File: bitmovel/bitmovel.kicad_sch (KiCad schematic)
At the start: 19 parts, among them J1 Conn_01x02_Male, J2 micro:bit, J3 motor D, J4 motor E, J5 Conn_01x02_Female, J6 Conn_01x02_Female, J7 Conn_01x01_Female, J8 Conn_01x01_Female, SW1 SW_SPST, U1 LM1117-3.3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

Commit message: Inclui ilhas para conectar a Vin
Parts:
- added J9: Conn_01x02_Female, Connector_PinHeader_2.54mm:PinHeader_1x02_P2.54mm_Vertical, symbol Connector:Conn_01x02_Female
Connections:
- net Vin: now also J9.1 (Pin_1), J9.2 (Pin_2)
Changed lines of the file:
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@@
+    (stroke (width 0) (type default) (color 0 0 0 0))
+  )
+  (wire (pts (xy 115.57 103.505) (xy 115.57 106.045))
     (stroke (width 0) (type default) (color 0 0 0 0))
   )
@@
   )
   (label "3.3V" (at 147.32 113.03 0)
+    (effects (font (size 1.27 1.27)) (justify left bottom))
+  )
+  (label "Vin" (at 115.57 105.41 0)
     (effects (font (size 1.27 1.27)) (justify left bottom))
   )
@@
     (pin "1")
   )
+  (symbol (lib_id "Connector:Conn_01x02_Female") (at 110.49 103.505 0) (mirror y) (unit 1)
+    (in_bom yes) (on_board yes) (fields_autoplaced)
+    (property "Reference" "J9" (id 0) (at 111.125 97.79 0)
+      (effects (font (size 1.27 1.27)) hide)
+    )
+    (property "Value" "Conn_01x02_Female" (id 1) (at 111.125 100.33 0)
+      (effects (font (size 1.27 1.27)) hide)
+    )
+    (property "Footprint" "Connector_PinHeader_2.54mm:PinHeader_1x02_P2.54mm_Vertical" (id 2) (at 110.49 103.505 0)
+      (effects (font (size 1.27 1.27)) hide)
+    )
+    (property "Datasheet" "~" (id 3) (at 110.49 103.505 0)
+      (effects (font (size 1.27 1.27)) hide)
+    )
+    (pin "1")
+    (pin "2")
+  )
   (symbol (lib_id "Connector:Conn_01x02_Female") (at 110.49 116.205 0) (mirror y) (unit 1)
     (in_bom yes) (on_board yes) (fields_autoplaced)
@@
       (reference "J8") (unit 1) (value "Conn_01x01_Female") (footprint "Connector_PinHeader_2.54mm:PinHeader_1x01_P2.54mm_Vertical")
     )
+    (path "/dde3811c-ee13-425b-b5d6-76051d186440"
+      (reference "J9") (unit 1) (value "Conn_01x02_Female") (footprint "Connector_PinHeader_2.54mm:PinHeader_1x02_P2.54mm_Vertical")
+    )
     (path "/00000000-0000-0000-0000-00005ffbb56c"

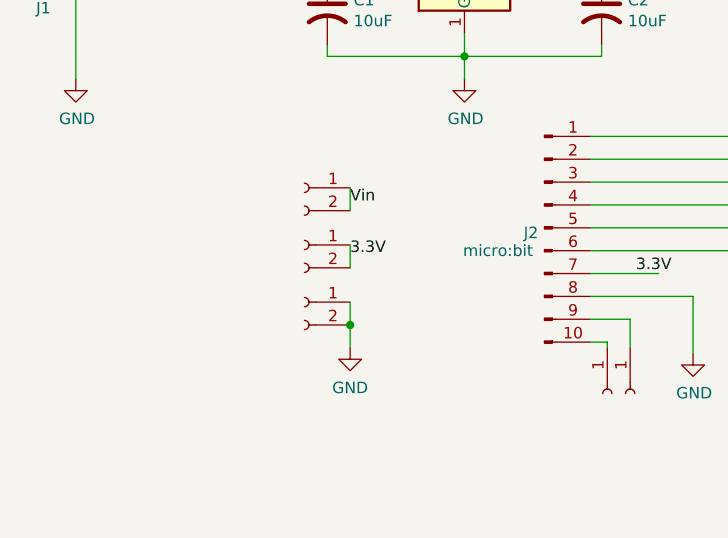
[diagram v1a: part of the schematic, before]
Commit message: Corrige posição das ilhas 3v3 e GND
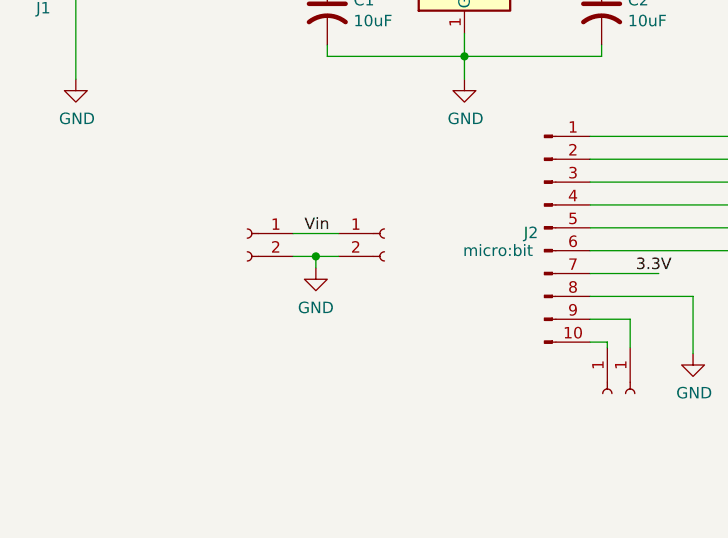
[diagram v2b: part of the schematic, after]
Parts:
- removed J5: Conn_01x02_Female, Connector_PinHeader_2.54mm:PinHeader_1x02_P2.54mm_Vertical, symbol Connector:Conn_01x02_Female
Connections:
- net GND: now also J9.2 (Pin_2); no longer J6.1 (Pin_1)
- net Vin: now also J6.1 (Pin_1); no longer J9.2 (Pin_2)
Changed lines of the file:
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@@
   (junction (at 128.27 88.9) (diameter 0) (color 0 0 0 0)
   )
-  (junction (at 115.57 118.745) (diameter 0) (color 0 0 0 0)
-  )
   (junction (at 113.03 78.74) (diameter 0) (color 0 0 0 0)
   )
@@
   (junction (at 147.32 69.85) (diameter 0) (color 0 0 0 0)
   )
+  (junction (at 111.76 111.125) (diameter 0) (color 0 0 0 0)
+  )
   (junction (at 175.26 129.54) (diameter 0) (color 0 0 0 0)
   )
@@
     (stroke (width 0) (type default) (color 0 0 0 0))
   )
-  (wire (pts (xy 115.57 116.205) (xy 115.57 118.745))
-    (stroke (width 0) (type default) (color 0 0 0 0))
-  )
   (wire (pts (xy 146.685 118.11) (xy 146.685 121.285))
     (stroke (width 0) (type default) (color 0 0 0 0))
   )
+  (wire (pts (xy 111.76 112.395) (xy 111.76 111.125))
+    (stroke (width 0) (type default) (color 0 0 0 0))
+  )
   (wire (pts (xy 113.03 78.74) (xy 113.03 69.85))
     (stroke (width 0) (type default) (color 0 0 0 0))
@@
     (stroke (width 0) (type default) (color 0 0 0 0))
   )
+  (wire (pts (xy 111.76 111.125) (xy 114.3 111.125))
+    (stroke (width 0) (type default) (color 0 0 0 0))
+  )
   (wire (pts (xy 142.24 110.49) (xy 158.75 110.49))
     (stroke (width 0) (type default) (color 0 0 0 0))
@@
     (stroke (width 0) (type default) (color 0 0 0 0))
   )
-  (wire (pts (xy 115.57 109.855) (xy 115.57 112.395))
-    (stroke (width 0) (type default) (color 0 0 0 0))
-  )
   (wire (pts (xy 182.88 129.54) (xy 182.88 128.27))
     (stroke (width 0) (type default) (color 0 0 0 0))
@@
     (stroke (width 0) (type default) (color 0 0 0 0))
   )
+  (wire (pts (xy 109.22 108.585) (xy 114.3 108.585))
+    (stroke (width 0) (type default) (color 0 0 0 0))
+  )
   (wire (pts (xy 172.72 129.54) (xy 175.26 129.54))
     (stroke (width 0) (type default) (color 0 0 0 0))
@@
     (stroke (width 0) (type default) (color 0 0 0 0))
   )
-  (wire (pts (xy 115.57 118.745) (xy 115.57 121.285))
-    (stroke (width 0) (type default) (color 0 0 0 0))
-  )
   (wire (pts (xy 161.29 92.71) (xy 165.1 92.71))
     (stroke (width 0) (type default) (color 0 0 0 0))
@@
     (stroke (width 0) (type default) (color 0 0 0 0))
   )
-  (wire (pts (xy 115.57 103.505) (xy 115.57 106.045))
-    (stroke (width 0) (type default) (color 0 0 0 0))
-  )
   (wire (pts (xy 190.5 92.71) (xy 198.12 92.71))
     (stroke (width 0) (type default) (color 0 0 0 0))
@@
   )
   (wire (pts (xy 142.24 115.57) (xy 153.67 115.57))
+    (stroke (width 0) (type default) (color 0 0 0 0))
+  )
+  (wire (pts (xy 111.76 111.125) (xy 109.22 111.125))
     (stroke (width 0) (type default) (color 0 0 0 0))
   )
@@
     (effects (font (size 1.27 1.27)) (justify left bottom))
   )
-  (label "Vin" (at 115.57 105.41 0)
-    (effects (font (size 1.27 1.27)) (justify left bottom))
-  )
-  (label "3.3V" (at 115.57 111.125 0)
+  (label "Vin" (at 110.49 108.585 0)
     (effects (font (size 1.27 1.27)) (justify left bottom))
   )
@@
     (pin "1")
   )
-  (symbol (lib_id "Connector:Conn_01x02_Female") (at 110.49 109.855 0) (mirror y) (unit 1)
+  (symbol (lib_id "power:GND") (at 111.76 112.395 0) (unit 1)
     (in_bom yes) (on_board yes) (fields_autoplaced)
-    (property "Reference" "J5" (id 0) (at 111.125 104.14 0)
-      (effects (font (size 1.27 1.27)) hide)
-    )
-    (property "Value" "Conn_01x02_Female" (id 1) (at 111.125 106.68 0)
-      (effects (font (size 1.27 1.27)) hide)
-    )
-    (property "Footprint" "Connector_PinHeader_2.54mm:PinHeader_1x02_P2.54mm_Vertical" (id 2) (at 110.49 109.855 0)
-      (effects (font (size 1.27 1.27)) hide)
-    )
-    (property "Datasheet" "~" (id 3) (at 110.49 109.855 0)
-      (effects (font (size 1.27 1.27)) hide)
-    )
-    (pin "1")
-    (pin "2")
-  )
-  (symbol (lib_id "power:GND") (at 115.57 121.285 0) (unit 1)
-    (in_bom yes) (on_board yes) (fields_autoplaced)
-    (property "Reference" "#PWR03" (id 0) (at 115.57 127.635 0)
-      (effects (font (size 1.27 1.27)) hide)
-    )
-    (property "Value" "GND" (id 1) (at 115.57 125.73 0))
-    (property "Footprint" "" (id 2) (at 115.57 121.285 0)
-      (effects (font (size 1.27 1.27)) hide)
-    )
-    (property "Datasheet" "" (id 3) (at 115.57 121.285 0)
+    (property "Reference" "#PWR03" (id 0) (at 111.76 118.745 0)
+      (effects (font (size 1.27 1.27)) hide)
+    )
+    (property "Value" "GND" (id 1) (at 111.76 116.84 0))
+    (property "Footprint" "" (id 2) (at 111.76 112.395 0)
+      (effects (font (size 1.27 1.27)) hide)
+    )
+    (property "Datasheet" "" (id 3) (at 111.76 112.395 0)
       (effects (font (size 1.27 1.27)) hide)
     )
@@
     (pin "1")
   )
-  (symbol (lib_id "Connector:Conn_01x02_Female") (at 110.49 103.505 0) (mirror y) (unit 1)
+  (symbol (lib_id "Connector:Conn_01x02_Female") (at 119.38 108.585 0) (unit 1)
     (in_bom yes) (on_board yes) (fields_autoplaced)
-    (property "Reference" "J9" (id 0) (at 111.125 97.79 0)
-      (effects (font (size 1.27 1.27)) hide)
-    )
-    (property "Value" "Conn_01x02_Female" (id 1) (at 111.125 100.33 0)
-      (effects (font (size 1.27 1.27)) hide)
-    )
-    (property "Footprint" "Connector_PinHeader_2.54mm:PinHeader_1x02_P2.54mm_Vertical" (id 2) (at 110.49 103.505 0)
-      (effects (font (size 1.27 1.27)) hide)
-    )
-    (property "Datasheet" "~" (id 3) (at 110.49 103.505 0)
-      (effects (font (size 1.27 1.27)) hide)
-    )
-    (pin "1")
-    (pin "2")
-  )
-  (symbol (lib_id "Connector:Conn_01x02_Female") (at 110.49 116.205 0) (mirror y) (unit 1)
+    (property "Reference" "J9" (id 0) (at 118.745 102.87 0)
+      (effects (font (size 1.27 1.27)) hide)
+    )
+    (property "Value" "Conn_01x02_Female" (id 1) (at 118.745 105.41 0)
+      (effects (font (size 1.27 1.27)) hide)
+    )
+    (property "Footprint" "Connector_PinHeader_2.54mm:PinHeader_1x02_P2.54mm_Vertical" (id 2) (at 119.38 108.585 0)
+      (effects (font (size 1.27 1.27)) hide)
+    )
+    (property "Datasheet" "~" (id 3) (at 119.38 108.585 0)
+      (effects (font (size 1.27 1.27)) hide)
+    )
+    (pin "1")
+    (pin "2")
+  )
+  (symbol (lib_id "Connector:Conn_01x02_Female") (at 104.14 108.585 0) (mirror y) (unit 1)
     (in_bom yes) (on_board yes) (fields_autoplaced)
-    (property "Reference" "J6" (id 0) (at 111.125 110.49 0)
-      (effects (font (size 1.27 1.27)) hide)
-    )
-    (property "Value" "Conn_01x02_Female" (id 1) (at 111.125 113.03 0)
-      (effects (font (size 1.27 1.27)) hide)
-    )
-    (property "Footprint" "Connector_PinHeader_2.54mm:PinHeader_1x02_P2.54mm_Vertical" (id 2) (at 110.49 116.205 0)
-      (effects (font (size 1.27 1.27)) hide)
-    )
-    (property "Datasheet" "~" (id 3) (at 110.49 116.205 0)
+    (property "Reference" "J6" (id 0) (at 104.775 102.87 0)
+      (effects (font (size 1.27 1.27)) hide)
+    )
+    (property "Value" "Conn_01x02_Female" (id 1) (at 104.775 105.41 0)
+      (effects (font (size 1.27 1.27)) hide)
+    )
+    (property "Footprint" "Connector_PinHeader_2.54mm:PinHeader_1x02_P2.54mm_Vertical" (id 2) (at 104.14 108.585 0)
+      (effects (font (size 1.27 1.27)) hide)
+    )
+    (property "Datasheet" "~" (id 3) (at 104.14 108.585 0)
       (effects (font (size 1.27 1.27)) hide)
     )
@@
       (reference "J4") (unit 1) (value "motor E") (footprint "bitmovel:SolderJumper-2_P1.3mm_Open_RoundedPad1.0x1.5mm")
     )
-    (path "/67b618a0-4e81-4810-b403-b96fb65bbb0d"
-      (reference "J5") (unit 1) (value "Conn_01x02_Female") (footprint "Connector_PinHeader_2.54mm:PinHeader_1x02_P2.54mm_Vertical")
-    )
     (path "/f05c9b19-6ba3-4bcf-ad4b-954d208c6150"
